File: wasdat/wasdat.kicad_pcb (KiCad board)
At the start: 2 copper layers, 55.5 x 33 mm, 20 parts, among them J1 ISP, U1 ATmega32U4, U2 74HC138, X1 16mhz

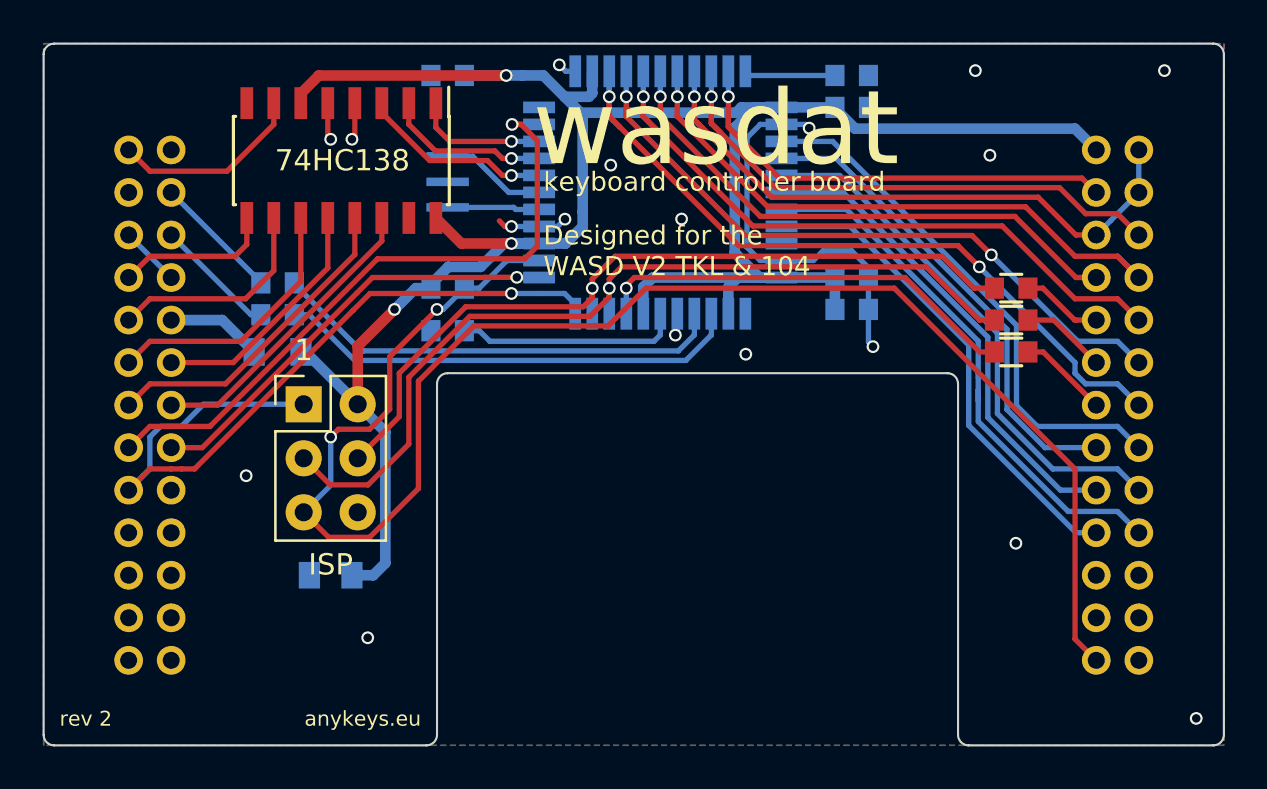
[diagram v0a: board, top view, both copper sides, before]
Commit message: Fixing a cleaner version that is cheaper to produce.
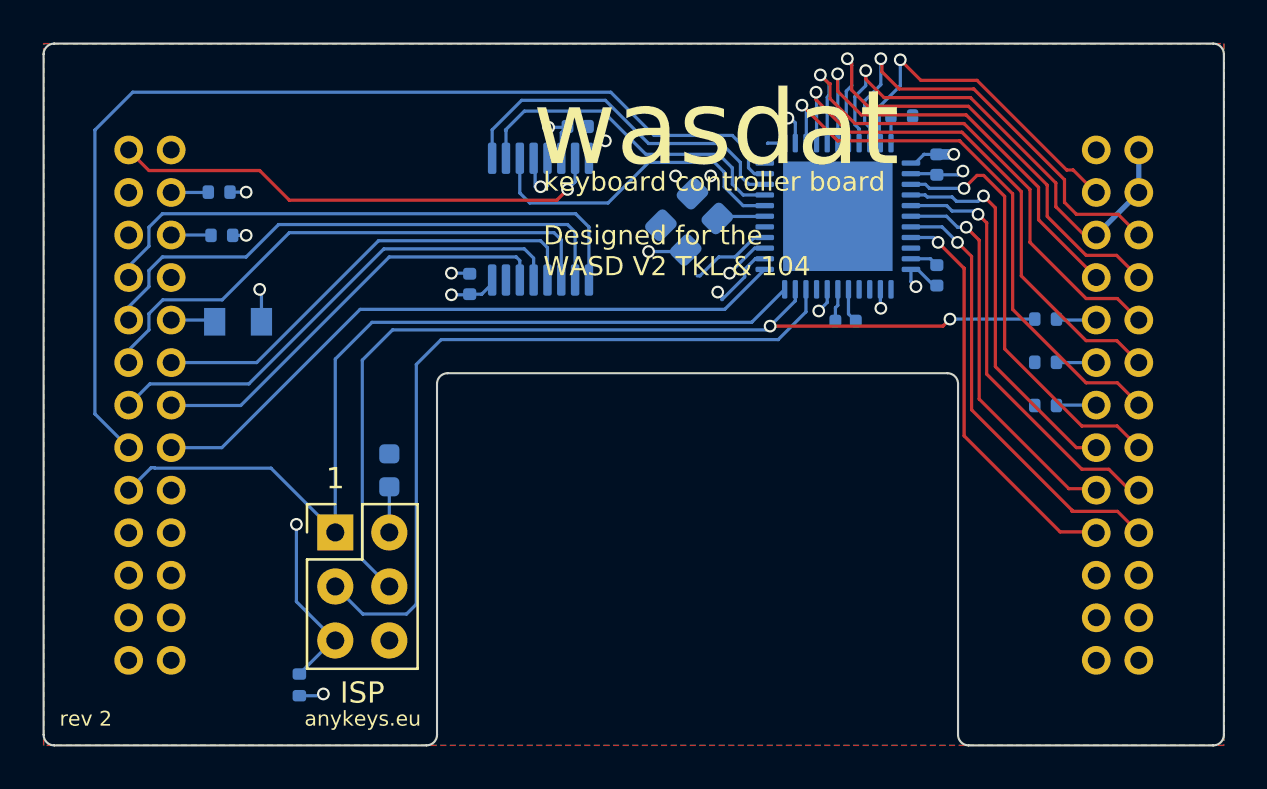
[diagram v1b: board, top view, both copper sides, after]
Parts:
- removed X1: 16mhz, Keeb_components:Resonator_SMD_muRata_CSTNExxV-3Pin-p1.2
- added Y2: ASCO, Oscillator:Oscillator_SMD_Abracon_ASE-4Pin_3.2x2.5mm, B.Cu at (30.4, 8.38)
- C1, C2, C3, C4, C6: footprint Keeb_components:C_0603 -> Capacitor_SMD:C_0402_1005Metric
- C5: footprint Keeb_components:C_0805 -> Capacitor_SMD:C_0603_1608Metric
- R1, R2, R3, R4: footprint Keeb_components:R_0603 -> Resistor_SMD:R_0402_1005Metric
- R5, R6, R7: footprint Keeb_components:R_0603 -> Resistor_SMD:R_0402_1005Metric; moved to B.Cu
- U1: footprint Keeb_components:ATMEGA32U4 -> Package_DFN_QFN:QFN-44-1EP_7x7mm_P0.5mm_EP5.15x5.15mm
- U2: footprint Package_SO:SOIC-16_3.9x9.9mm_P1.27mm -> Package_SO:TSSOP-16_4.4x5mm_P0.65mm; moved to B.Cu
- moved R3 19.9 mm to (12.0, 30.2), turned to 90 degrees
- moved C6 18.7 mm to (37.7, 13.1), turned to 0 degrees
- moved C3 18.0 mm to (20.0, 11.3), turned to 90 degrees
- moved U2 9.76 mm to (23.4, 8.26)
- moved U1 8.42 mm to (37.3, 8.12)
- moved C1 6.57 mm to (25.1, 3.90), turned to 0 degrees
- moved J1 6.21 mm to (15.0, 25.5)
- moved C5 5.65 mm to (16.3, 20.1), turned to 90 degrees
- moved R1 5.07 mm to (8.26, 6.99)
- moved C2 4.82 mm to (42.0, 5.69), turned to -90 degrees
- moved R2 4.56 mm to (8.38, 9.02)
- moved C4 4.00 mm to (42.0, 10.9), turned to 90 degrees
- moved R4 3.03 mm to (40.4, 3.40)
- moved R7 2.99 mm to (47.1, 17.0)
- moved R6 2.56 mm to (47.1, 15.0)
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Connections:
- H1 pad 18: (no net) -> unconnected-(H1-Pin_18-Pad18)
- H1 pad 20: (no net) -> unconnected-(H1-Pin_20-Pad20)
- H1 pad 21: (no net) -> unconnected-(H1-Pin_21-Pad21)
- H1 pad 22: (no net) -> unconnected-(H1-Pin_22-Pad22)
- H1 pad 23: (no net) -> unconnected-(H1-Pin_23-Pad23)
- H1 pad 24: (no net) -> unconnected-(H1-Pin_24-Pad24)
- H1 pad 25: (no net) -> unconnected-(H1-Pin_25-Pad25)
- H1 pad 26: (no net) -> unconnected-(H1-Pin_26-Pad26)
- H2 pad 21: (no net) -> DIP_5
- H2 pad 22: (no net) -> DIP_6
- H2 pad 23: (no net) -> DIP_3
- H2 pad 24: (no net) -> DIP_4
- H2 pad 26: (no net) -> DIP_2
- U1 pad 1: (no net) -> unconnected-(U1-(INT6/AIN0)PE6-Pad1)
- U1 pad 16: Net-(U1-Pad16) -> unconnected-(U1-XTAL2-Pad16)
- U1 pad 22: (no net) -> unconnected-(U1-(XCK1/~{CTS})PD5-Pad22)
- U1 pad 42: (no net) -> unconnected-(U1-AREF-Pad42)
- U2 pad 15: (no net) -> unconnected-(U2-Y0-Pad15)
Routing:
- net VCC: track 110.3 -> 21.8 mm, vias 3 -> 11
- net DIP_1: track 76.3 -> 12.0 mm
- net Net-(U1-D-): track 22.0 -> 0.63 mm, vias 0 -> 1
- net Net-(U1-D+): track 21.5 -> 0.76 mm, vias 0 -> 1
- net LED_caps: track 20.2 -> 0.00 mm, vias 1 -> 0
- net col7: track 7.44 -> 26.5 mm
- net col13: track 30.9 -> 49.9 mm, vias 1 -> 0
- net col8: track 10.3 -> 26.1 mm
- net GND: track 30.3 -> 14.5 mm, vias 18 -> 6
- net col6: track 9.15 -> 23.5 mm, vias 0 -> 1
- net col9: track 12.7 -> 25.7 mm
- net col14: track 20.6 -> 31.4 mm, vias 1 -> 0
- net A0: track 6.27 -> 16.7 mm, vias 1 -> 0
- net col10: track 11.6 -> 21.7 mm
- net Net-(U1-UCAP): track 10.5 -> 1.55 mm
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- added copper zone on In1.Cu, net VCC
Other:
- copper layers 2 -> 4

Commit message: More clean up
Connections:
- net Net-(U1-D+) renamed /USB_D_P
- net Net-(U1-D-) renamed /USB_D_M
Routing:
- net GND: track 14.5 -> 17.2 mm
- net /USB_D_M: track 0.63 -> 3.16 mm, vias 1 -> 2
- net /USB_D_P: track 0.76 -> 2.86 mm, vias 1 -> 2
- net VCC: track 21.8 -> 20.9 mm
- net LED_num: track 45.8 -> 46.5 mm
- added copper zone on B.Cu, net VCC

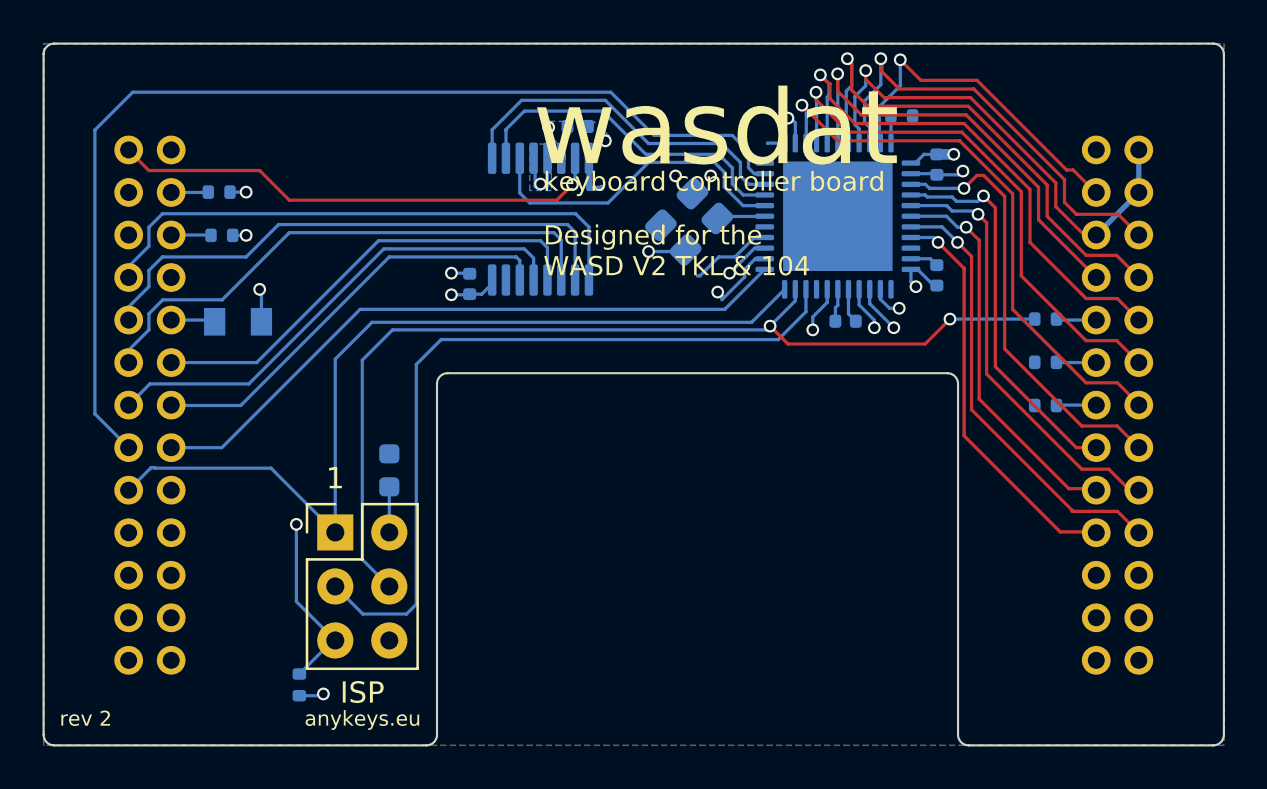
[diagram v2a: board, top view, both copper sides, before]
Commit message: Final updates, added 2 dip sw for user usage.
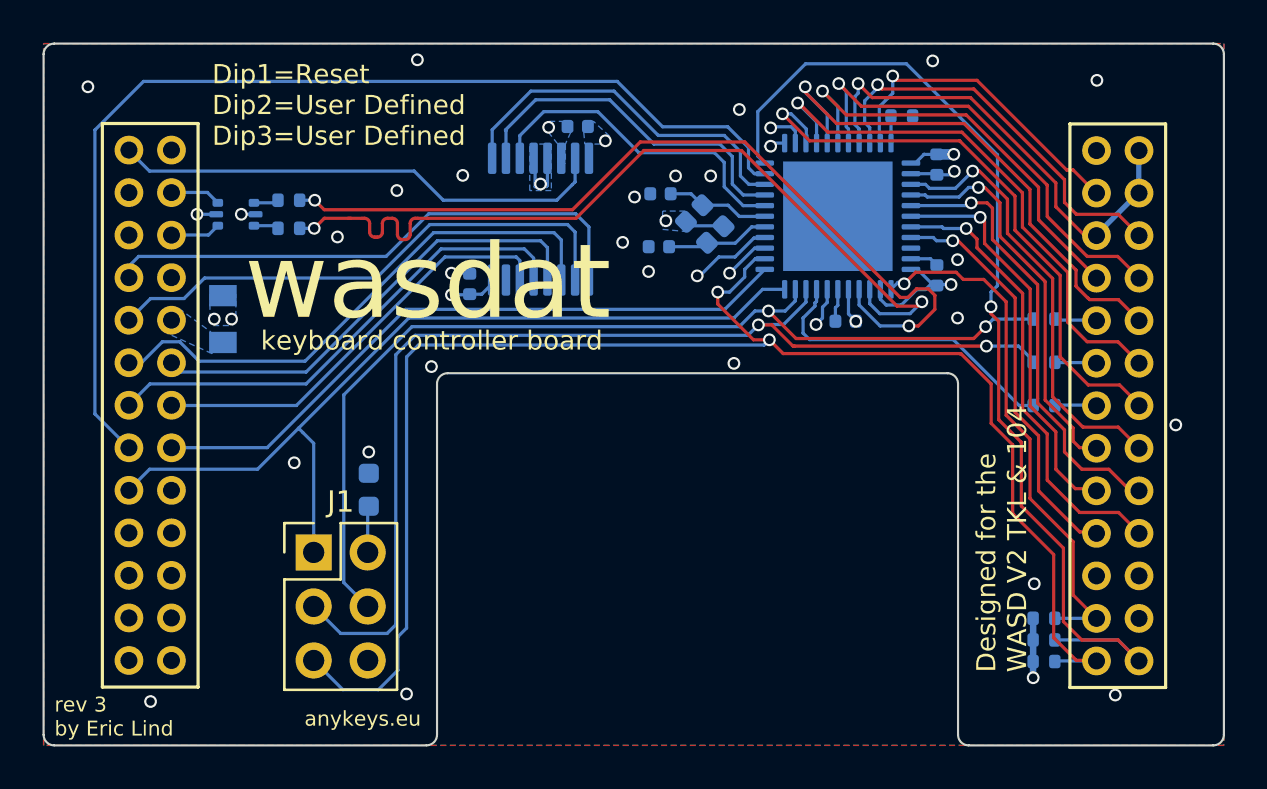
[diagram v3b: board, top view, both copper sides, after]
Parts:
- removed Y2: ASCO, Oscillator:Oscillator_SMD_Abracon_ASE-4Pin_3.2x2.5mm
- added C7: 12pF, Capacitor_SMD:C_0402_1005Metric, B.Cu at (29.0, 7.06)
- added C8: 12pF, Capacitor_SMD:C_0402_1005Metric, B.Cu at (28.9, 9.55)
- added R8: 10k, Resistor_SMD:R_0402_1005Metric, B.Cu at (47.0, 28.0)
- added R9: 10k, Resistor_SMD:R_0402_1005Metric, B.Cu at (47.0, 27.0)
- added U3: USBLC6-2P6, Package_TO_SOT_SMD:SOT-666, B.Cu at (9.04, 8.03)
- added Y1: 16MHz, Crystal:Crystal_SMD_2016-4Pin_2.0x1.6mm, B.Cu at (31.1, 8.48)
- H1, H2: moved to B.Cu
- J1: footprint Keeb_components:isp_standard -> Connector_PinHeader_2.54mm:PinHeader_2x03_P2.54mm_Vertical
- moved R3 35.0 mm to (47.0, 29.1), turned to 0 degrees
- moved R1 3.30 mm to (11.5, 7.37)
- moved R2 3.17 mm to (11.5, 8.69)
- moved J1 2.79 mm to (12.7, 23.9)
- moved H1 2.01 mm to (6.01, 5.01), turned to 180 degrees
- moved H2 2.01 mm to (51.5, 5.03), turned to 180 degrees
- moved C5 1.33 mm to (15.3, 21.0)
- moved F1 0.72 mm to (8.43, 13.0), turned to -90 degrees
- moved R5 0.07 mm to (47.0, 13.0)
- moved R6 0.07 mm to (47.0, 15.0)
- moved R7 0.07 mm to (47.0, 17.0)
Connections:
- net /USB_D_M renamed /USB_D_N
- F1 pad 2: Net-(H1-Pin_10) -> Net-(H1-Pin_9)
- H1 pad 1: col6 -> GND
- H1 pad 10: Net-(H1-Pin_10) -> col8
- H1 pad 11: col9 -> col10
- H1 pad 12: col10 -> col9
- H1 pad 13: col11 -> col12
- H1 pad 14: col12 -> col11
- H1 pad 15: col13 -> col14
- H1 pad 16: col14 -> col13
- H1 pad 17: MISO -> unconnected-(H1-Pin_17-Pad17)
- H1 pad 18: unconnected-(H1-Pin_18-Pad18) -> MISO
- H1 pad 19: GND -> unconnected-(H1-Pin_19-Pad19)
- H1 pad 2: GND -> col6
- H1 pad 20: unconnected-(H1-Pin_20-Pad20) -> GND
- H1 pad 3: GND -> D+
- H1 pad 4: D+ -> GND
- H1 pad 5: GND -> D-
- H1 pad 6: D- -> GND
- H1 pad 7: col7 -> GND
- H1 pad 8: GND -> col7
- H1 pad 9: col8 -> Net-(H1-Pin_9)
- H2 pad 1: VCC -> col1
- H2 pad 10: col5 -> Net-(H2-Pin_10)
- H2 pad 11: Net-(H2-Pin_11) -> row0
- H2 pad 12: row0 -> Net-(H2-Pin_12)
- H2 pad 13: Net-(H2-Pin_13) -> row1
- H2 pad 14: row1 -> Net-(H2-Pin_14)
- H2 pad 15: row2 -> row3
- H2 pad 16: row3 -> row2
- H2 pad 17: row4 -> row5
- H2 pad 18: row5 -> row4
- H2 pad 19: row6 -> row7
- H2 pad 2: col1 -> VCC
- H2 pad 20: row7 -> row6
- H2 pad 21: DIP_5 -> DIP_6
- H2 pad 22: DIP_6 -> DIP_5
- H2 pad 23: DIP_3 -> DIP_4
- H2 pad 24: DIP_4 -> DIP_3
- H2 pad 25: DIP_1 -> DIP_2
- H2 pad 26: DIP_2 -> DIP_1
- H2 pad 3: col0 -> col1
- H2 pad 4: col1 -> col0
- H2 pad 5: col1 -> col2
- H2 pad 6: col2 -> col1
- H2 pad 7: col3 -> col4
- H2 pad 8: col4 -> col3
- H2 pad 9: Net-(H2-Pin_9) -> col5
- R1 pad 2: D+ -> Net-(R1-Pad2)
- R2 pad 2: D- -> Net-(R2-Pad2)
- R5 pad 1: Net-(H2-Pin_9) -> Net-(H2-Pin_10)
- R6 pad 1: Net-(H2-Pin_11) -> Net-(H2-Pin_12)
- R7 pad 1: Net-(H2-Pin_13) -> Net-(H2-Pin_14)
- U1 pad 1: unconnected-(U1-(INT6/AIN0)PE6-Pad1) -> DIP_3
- U1 pad 16: unconnected-(U1-XTAL2-Pad16) -> Net-(U1-XTAL2)
- U1 pad 22: unconnected-(U1-(XCK1/~{CTS})PD5-Pad22) -> DIP_2
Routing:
- net DIP_1: track 12.0 -> 73.4 mm
- net DIP_2: track 0.00 -> 48.7 mm, vias 0 -> 1
- net /USB_D_P: track 2.86 -> 40.5 mm
- net /USB_D_N: track 3.16 -> 40.4 mm
- net DIP_3: track 0.00 -> 25.1 mm, vias 0 -> 1
- net LED_scroll: track 36.2 -> 51.9 mm, vias 0 -> 2
- net LED_caps: track 0.00 -> 14.6 mm
- net Net-(U1-XTAL2): track 0.00 -> 4.90 mm
- net Net-(U1-XTAL1): track 1.66 -> 4.87 mm
- net Net-(H1-Pin_10): track 2.08 -> 0.00 mm
- net col4: track 23.8 -> 21.7 mm
- net col2: track 20.9 -> 18.9 mm
- net Net-(H2-Pin_9): track 1.89 -> 0.00 mm
- net Net-(H2-Pin_10): track 0.00 -> 1.89 mm
- net Net-(H2-Pin_14): track 0.00 -> 1.88 mm
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- added copper zone on In2.Cu, net GND
- added copper zone on B.Cu, net Net-(H1-Pin_9)
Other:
- board text added: "Dip1=Reset Dip2=User Defined Dip3=User Defined"
- board text added: "rev 3 by Eric Lind"
- board text removed: "rev 2"
